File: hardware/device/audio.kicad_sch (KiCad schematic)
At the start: 28 parts, among them J10 HP_OUT, J5 AUDIO_EXP, J8 LINE_OUT, J9 LINE_IN, U1 FSA2466UMX, U29 NAU88C22YG

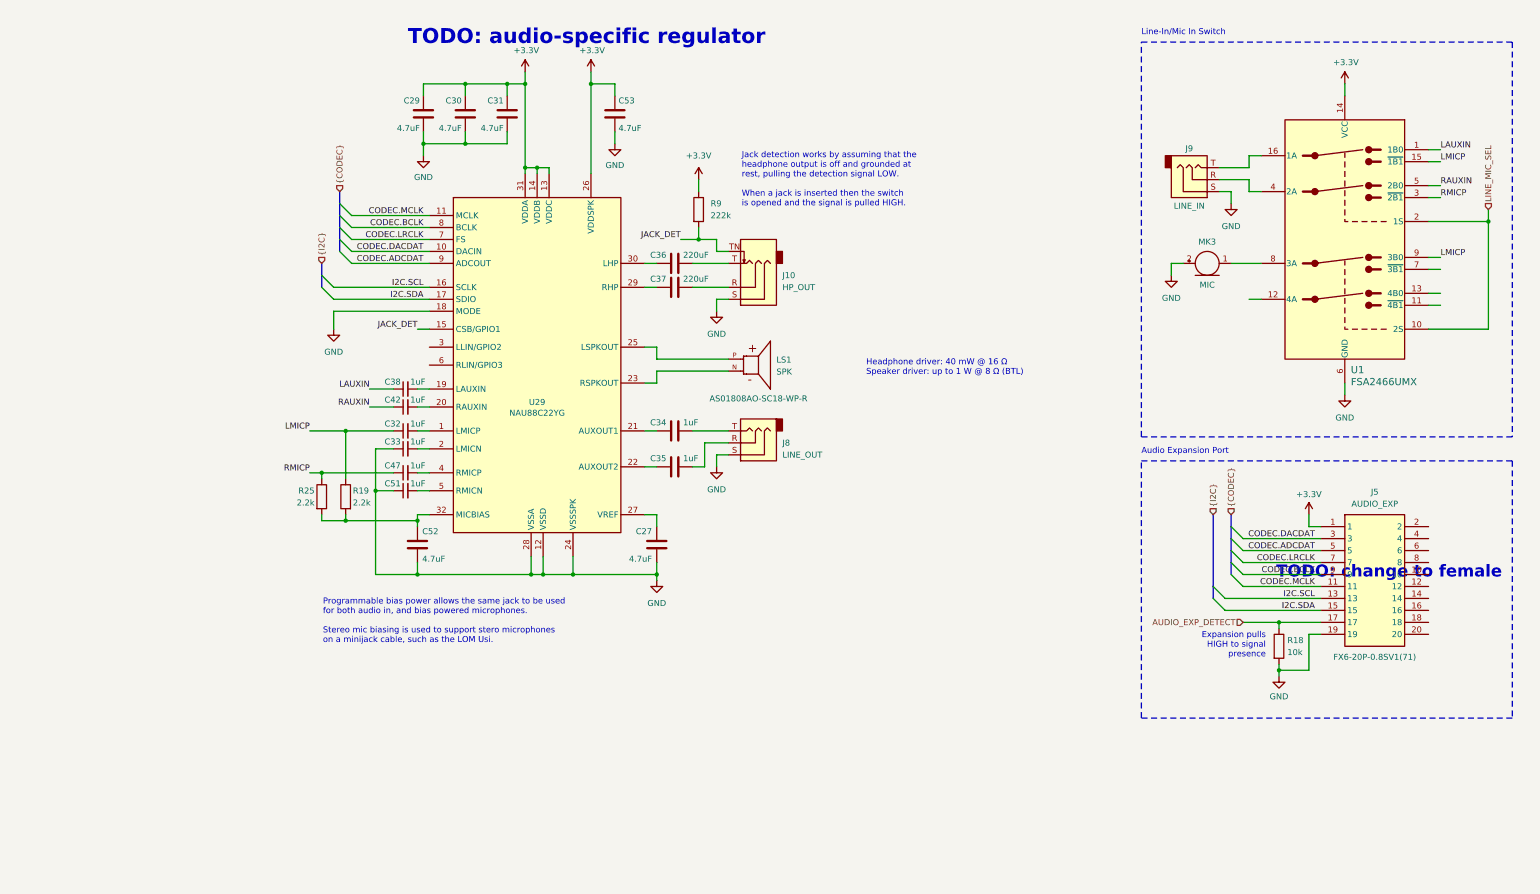
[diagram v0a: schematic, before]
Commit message: feat: add MEMs microphone
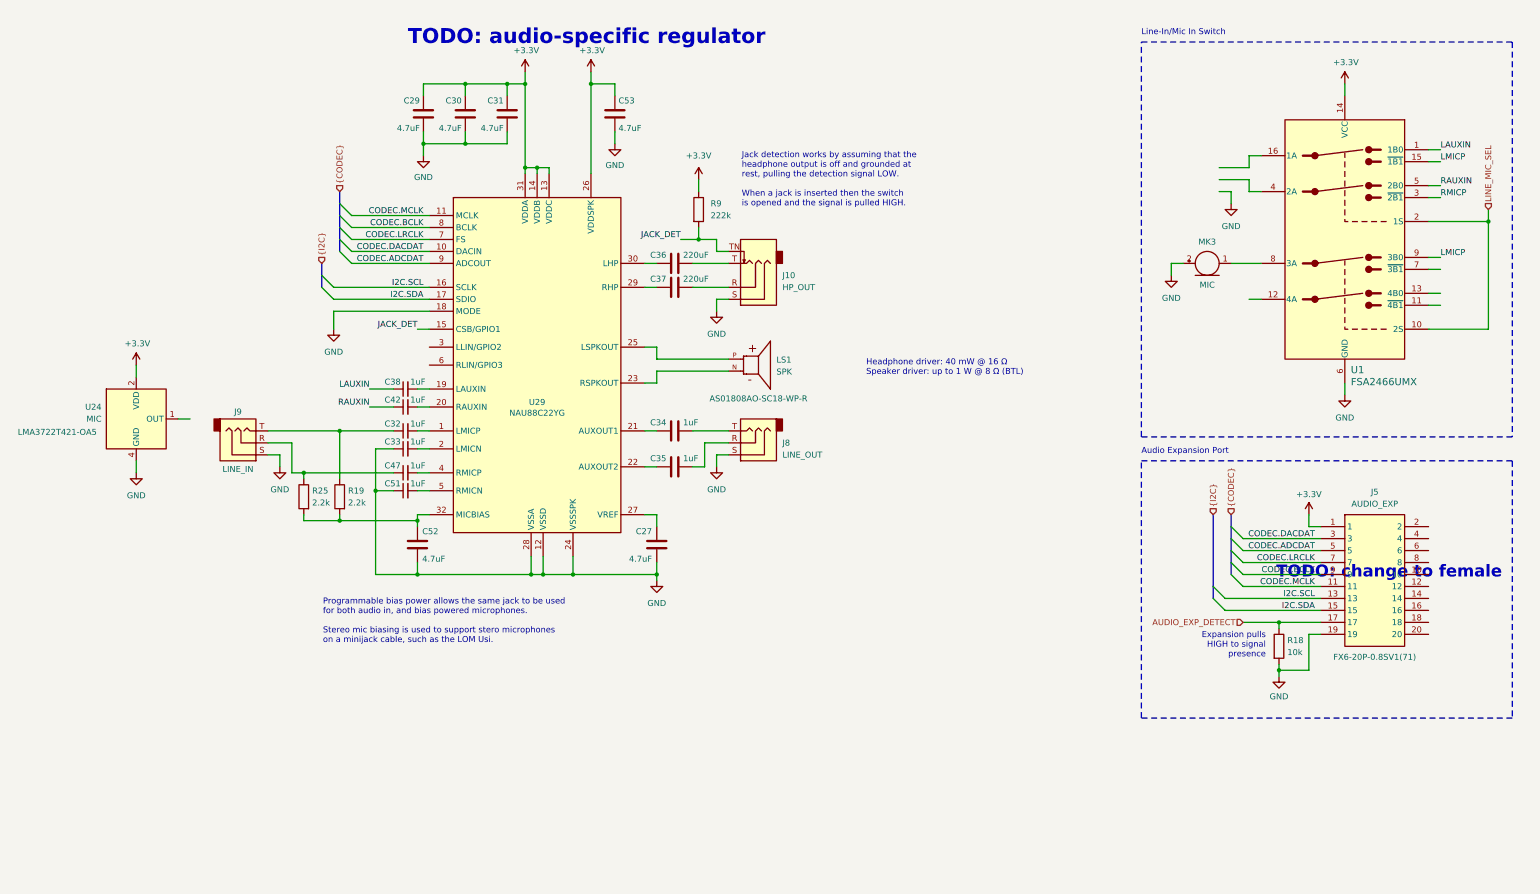
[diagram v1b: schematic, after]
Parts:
- added U24: MIC, pocket_synth:LMA3722T421-OA5, symbol pocket_synth:LMA3722T421-OA5
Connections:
- net +3.3V: now also U24.2 (VDD)
- net GND: now also U24.3 (GND), U24.4 (GND)
- net LMICP: no longer C32.1, R19.1
- net RMICP: no longer C47.1, R25.1
- net at J9.R: now also C47.1, R25.1; no longer U1.4 (2A)
- net at J9.T: now also C32.1, R19.1; no longer U1.16 (1A)
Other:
- moved on the sheet: J9, R19, R25

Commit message: feat: various PCB layout and routing
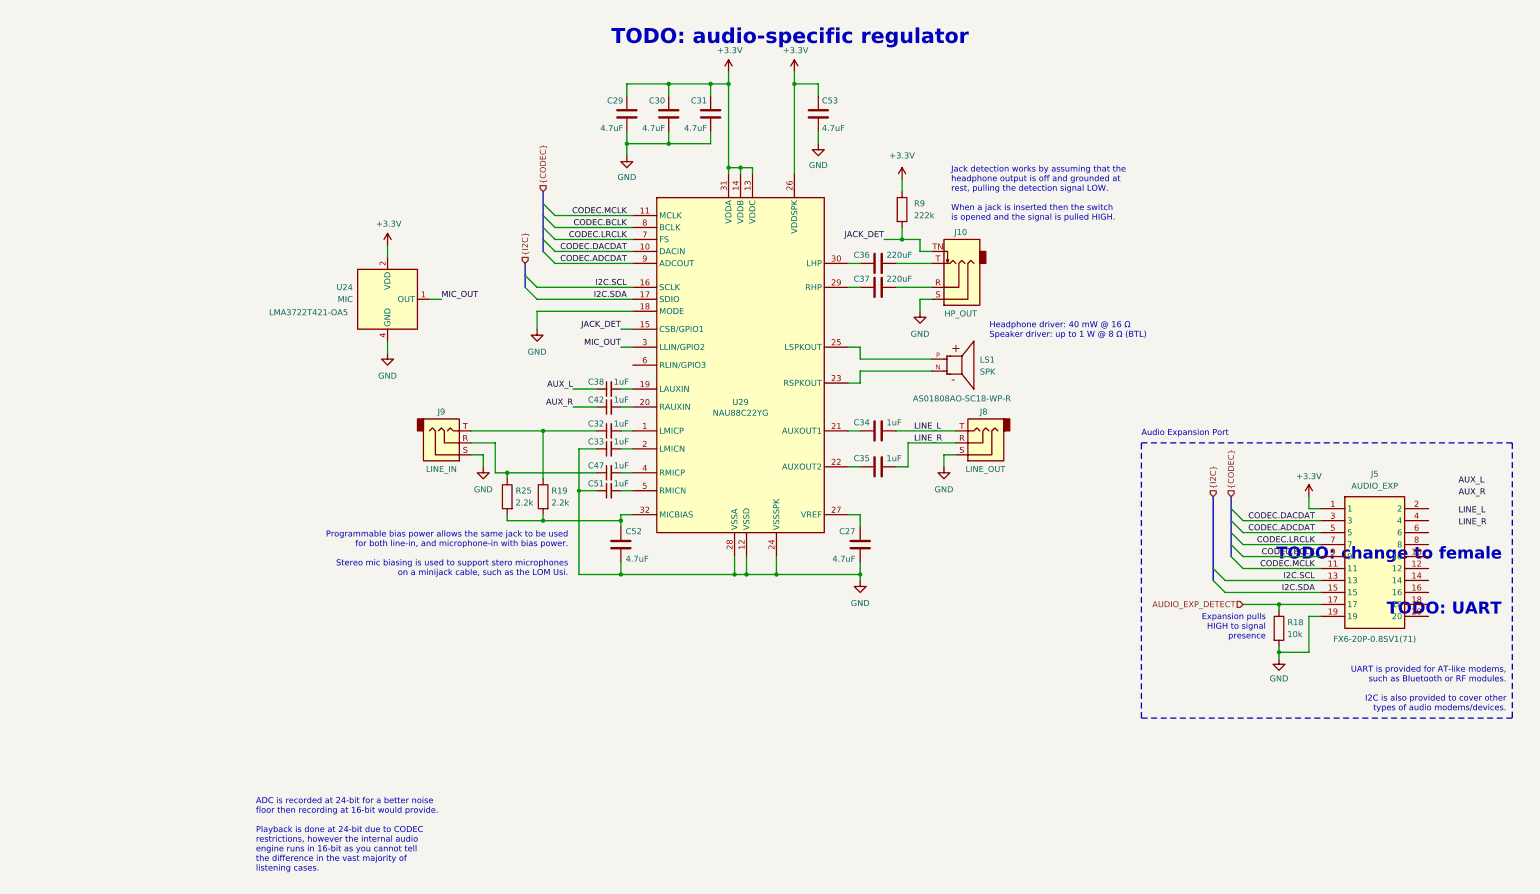
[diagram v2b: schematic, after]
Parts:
- removed MK3: MIC, symbol Device:Microphone
- removed U1: FSA2466UMX, pocket_synth:FSA2466UMX, symbol pocket_synth:FSA2466UMX
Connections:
- net LINE_R: now reaches C35.2, J8.R
- net LINE_L: now reaches C34.2, J8.T
- net MIC_OUT: now reaches U29.3 (LLIN/GPIO2)
- net MIC_OUT: now also U24.1 (OUT)
- net LAUXIN renamed AUX_L
- net RAUXIN renamed AUX_R
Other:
- note added: "ADC is recorded at 24-bit for a better noise floor then recording at 16-bit would provide. Playback is done at 24-bit due to CODEC restrictions, however the internal audio engine runs in 16-bit as you cannot tell the difference in the vast majority of listening cases."
- note added: "Programmable bias power allows the same jack to be used for both line-in, and microphone-in with bias power. Stereo mic biasing is used to support stero microphones on a minijack cable, such as the LOM Usi."
- note added: "TODO: UART"
- note added: "UART is provided for AT-like modems, such as Bluetooth or RF modules. I2C is also provided to cover other types of audio modems/devices."
- note removed: "Line-In/Mic In Switch"
- note removed: "Programmable bias power allows the same jack to be used for both audio in, and bias powered microphones. Stereo mic biasing is used to support stero microphones on a minijack cable, such as the LOM Usi."
- moved on the sheet: C27, C29, C30, C31, C32, C33, C34, C35, C36, C37, C38, C42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

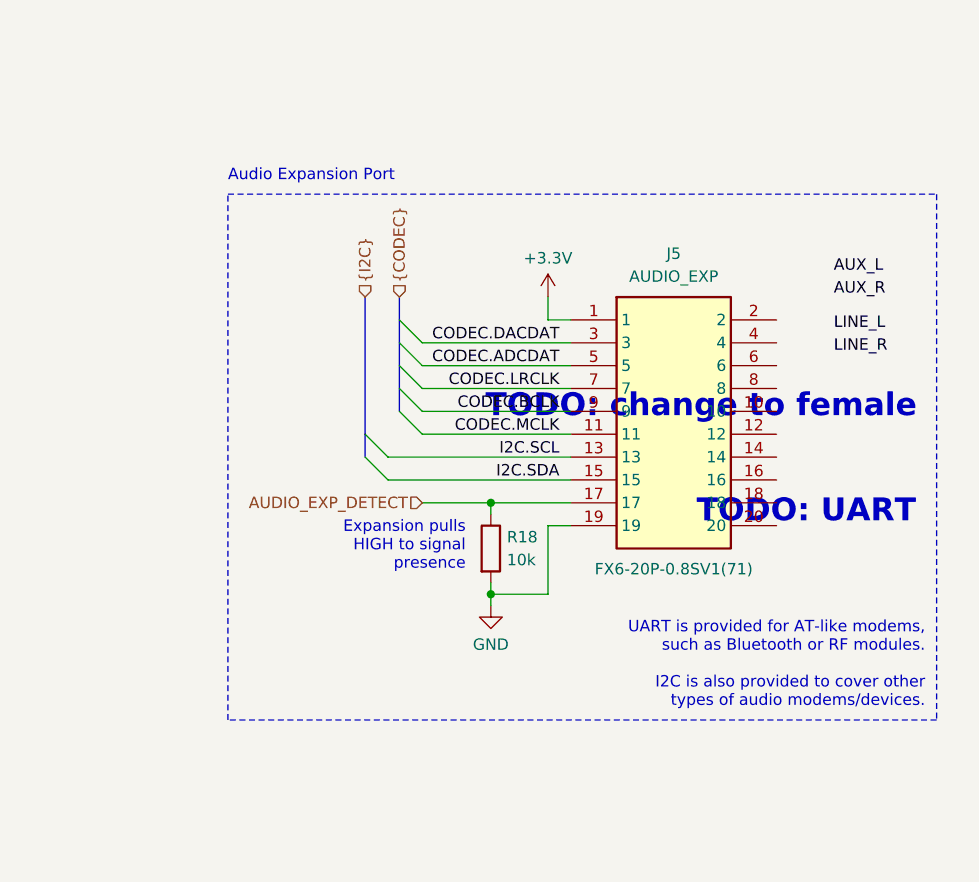
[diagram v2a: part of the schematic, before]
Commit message: chore: audio routing and UART port mapping
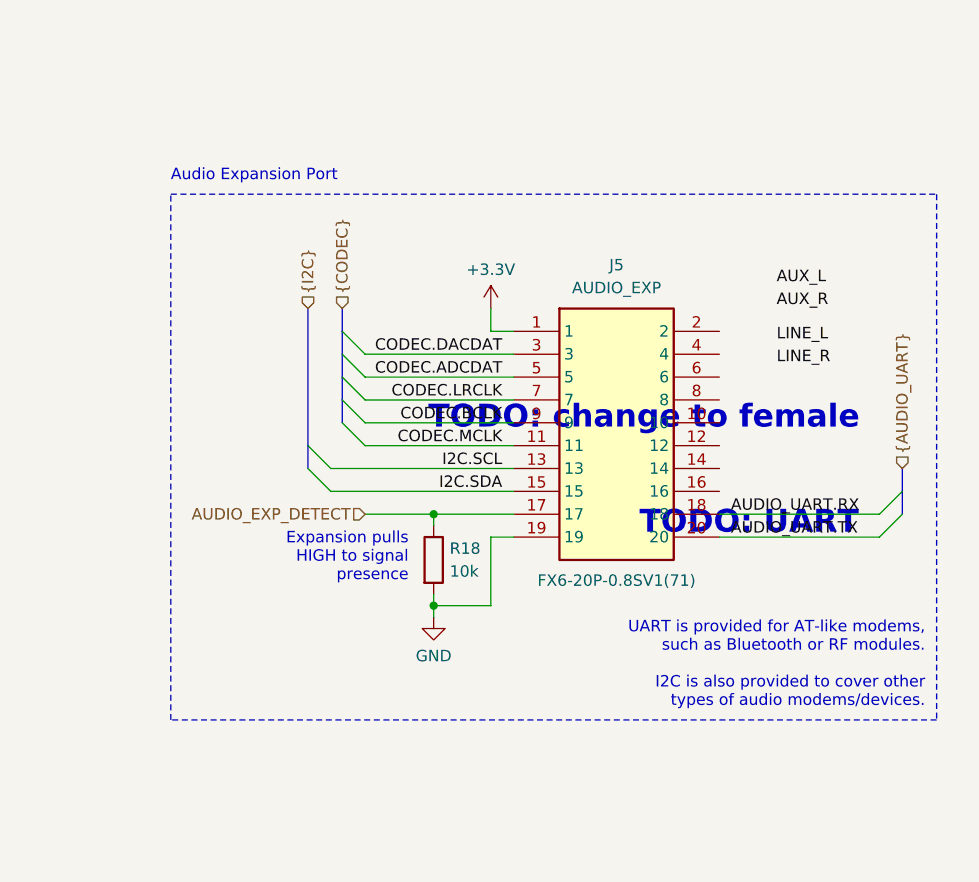
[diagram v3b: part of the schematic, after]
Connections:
- net AUDIO_UART.RX: now reaches J5.18
- net AUDIO_UART.TX: now reaches J5.20
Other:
- moved on the sheet: J5, R18

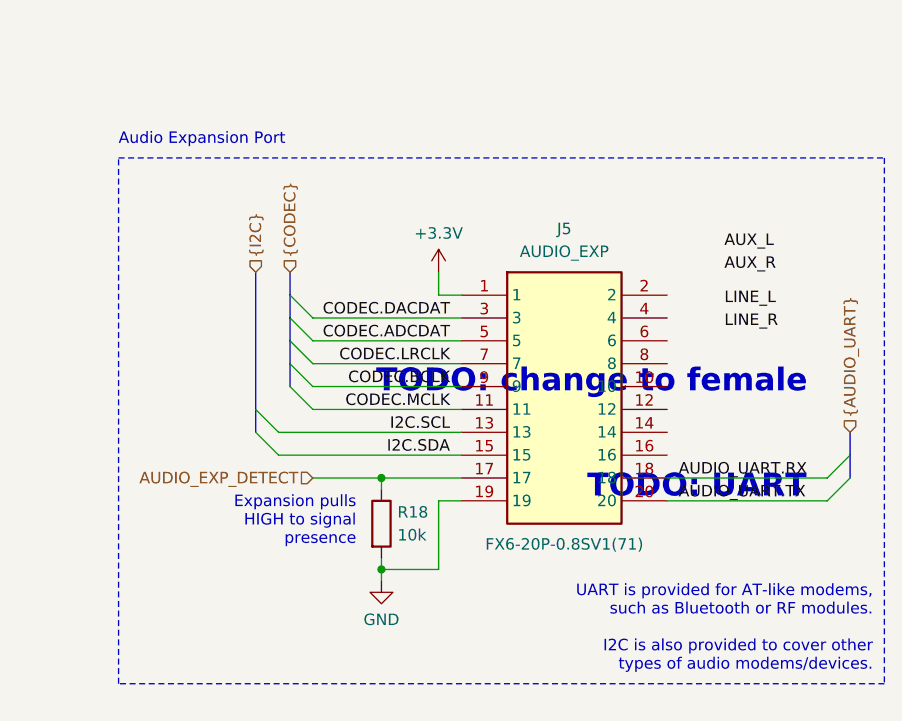
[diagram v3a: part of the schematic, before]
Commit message: fix: disconnected net buses
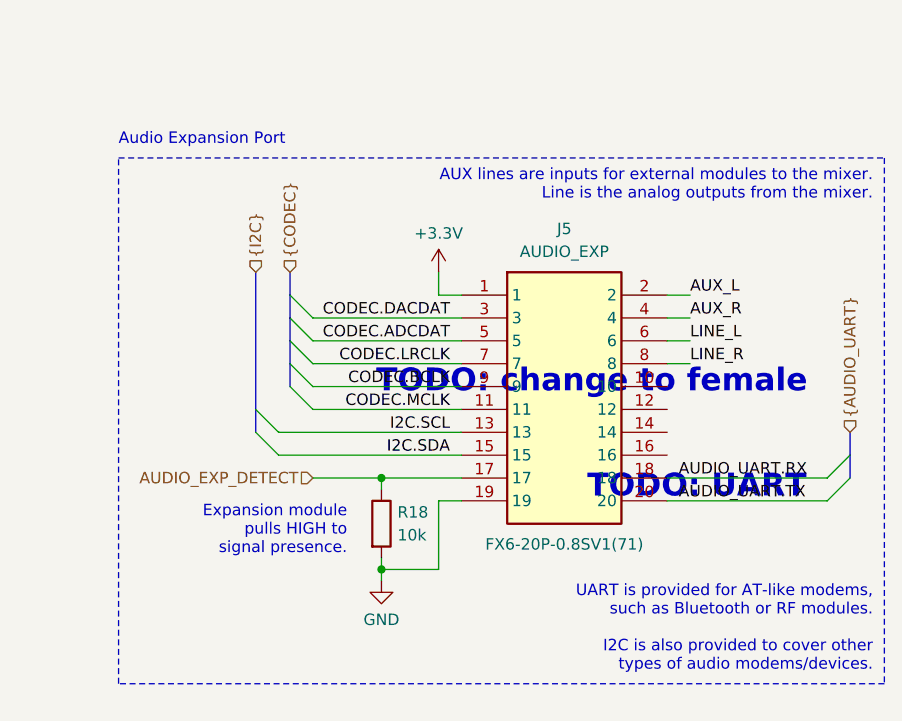
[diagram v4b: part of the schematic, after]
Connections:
- net AUX_L: now also J5.2
- net AUX_R: now also J5.4
- net LINE_L: now also J5.6
- net LINE_R: now also J5.8
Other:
- note added: "AUX lines are inputs for external modules to the mixer. Line is the analog outputs from the mixer."
- note added: "Expansion module pulls HIGH to signal presence."
- note removed: "Expansion pulls HIGH to signal presence"
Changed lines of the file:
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@@
 		)
 	)
-	(text "Expansion pulls\nHIGH to signal\npresence"
+	(text "Expansion module\npulls HIGH to\nsignal presence."
 		(exclude_from_sim no)
-		(at 221.996 144.526 0)
+		(at 220.98 145.542 0)
 		(effects
 			(font
@@
 		)
 	)
+	(text "AUX lines are inputs for external modules to the mixer.\nLine is the analog outputs from the mixer."
+		(exclude_from_sim no)
+		(at 279.4 105.41 0)
+		(effects
+			(font
+				(size 1.27 1.27)
+				(color 132 132 132 1)
+			)
+			(justify right top)
+		)
+	)
 	(text "Headphone driver: 40 mW @ 16 Ω\nSpeaker driver: up to 1 W @ 8 Ω (BTL)"
 		(exclude_from_sim no)
@@
 	(wire
 		(pts
+			(xy 256.54 119.38) (xy 259.08 119.38)
+		)
+		(stroke
+			(width 0)
+			(type default)
+		)
+	)
+	(wire
+		(pts
 			(xy 139.7 66.04) (xy 142.24 66.04)
 		)
@@
 	(wire
 		(pts
+			(xy 256.54 127) (xy 259.08 127)
+		)
+		(stroke
+			(width 0)
+			(type default)
+		)
+	)
+	(wire
+		(pts
 			(xy 114.3 46.99) (xy 114.3 45.72)
 		)
@@
 		(pts
 			(xy 114.3 25.4) (xy 114.3 27.94)
+		)
+		(stroke
+			(width 0)
+			(type default)
+		)
+	)
+	(wire
+		(pts
+			(xy 256.54 124.46) (xy 259.08 124.46)
+		)
+		(stroke
+			(width 0)
+			(type default)
+		)
+	)
+	(wire
+		(pts
+			(xy 256.54 121.92) (xy 259.08 121.92)
 		)
 		(stroke
@@
 	)
 	(label "LINE_L"
-		(at 262.89 120.65 0)
+		(at 259.08 124.46 0)
 		(effects
 			(font
@@
 	)
 	(label "AUX_L"
-		(at 262.89 114.3 0)
+		(at 259.08 119.38 0)
 		(effects
 			(font
@@
 	)
 	(label "LINE_R"
-		(at 262.89 123.19 0)
+		(at 259.08 127 0)
 		(effects
 			(font
@@
 	)
 	(label "AUX_R"
-		(at 262.89 116.84 0)
-		(effects
-			(font
+		(at 259.08 121.92 0)
+		(effects
+			(font
